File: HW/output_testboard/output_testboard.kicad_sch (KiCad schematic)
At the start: 50 parts, among them J1 IN, J2 OUT, J3 OUT, J4 DC_Jack, J5 9V, U1 TL072, U3 TL072

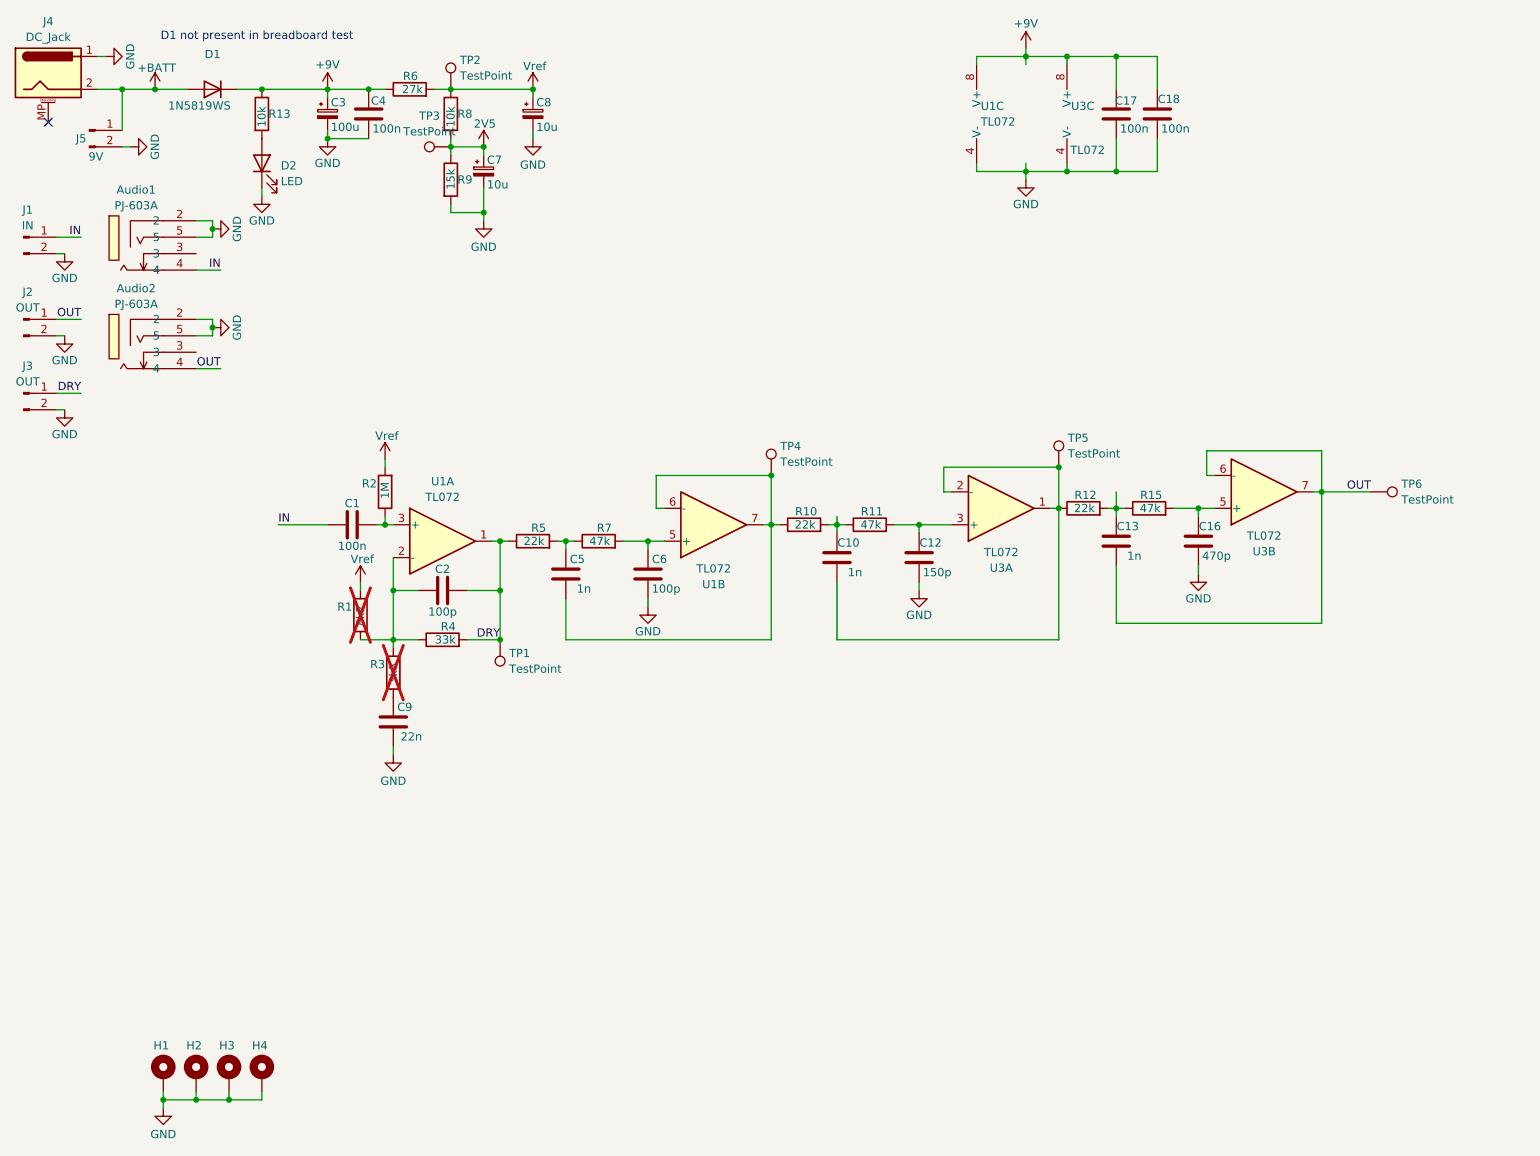
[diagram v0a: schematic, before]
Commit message: working passthrough code with dma + ouput buffer HW
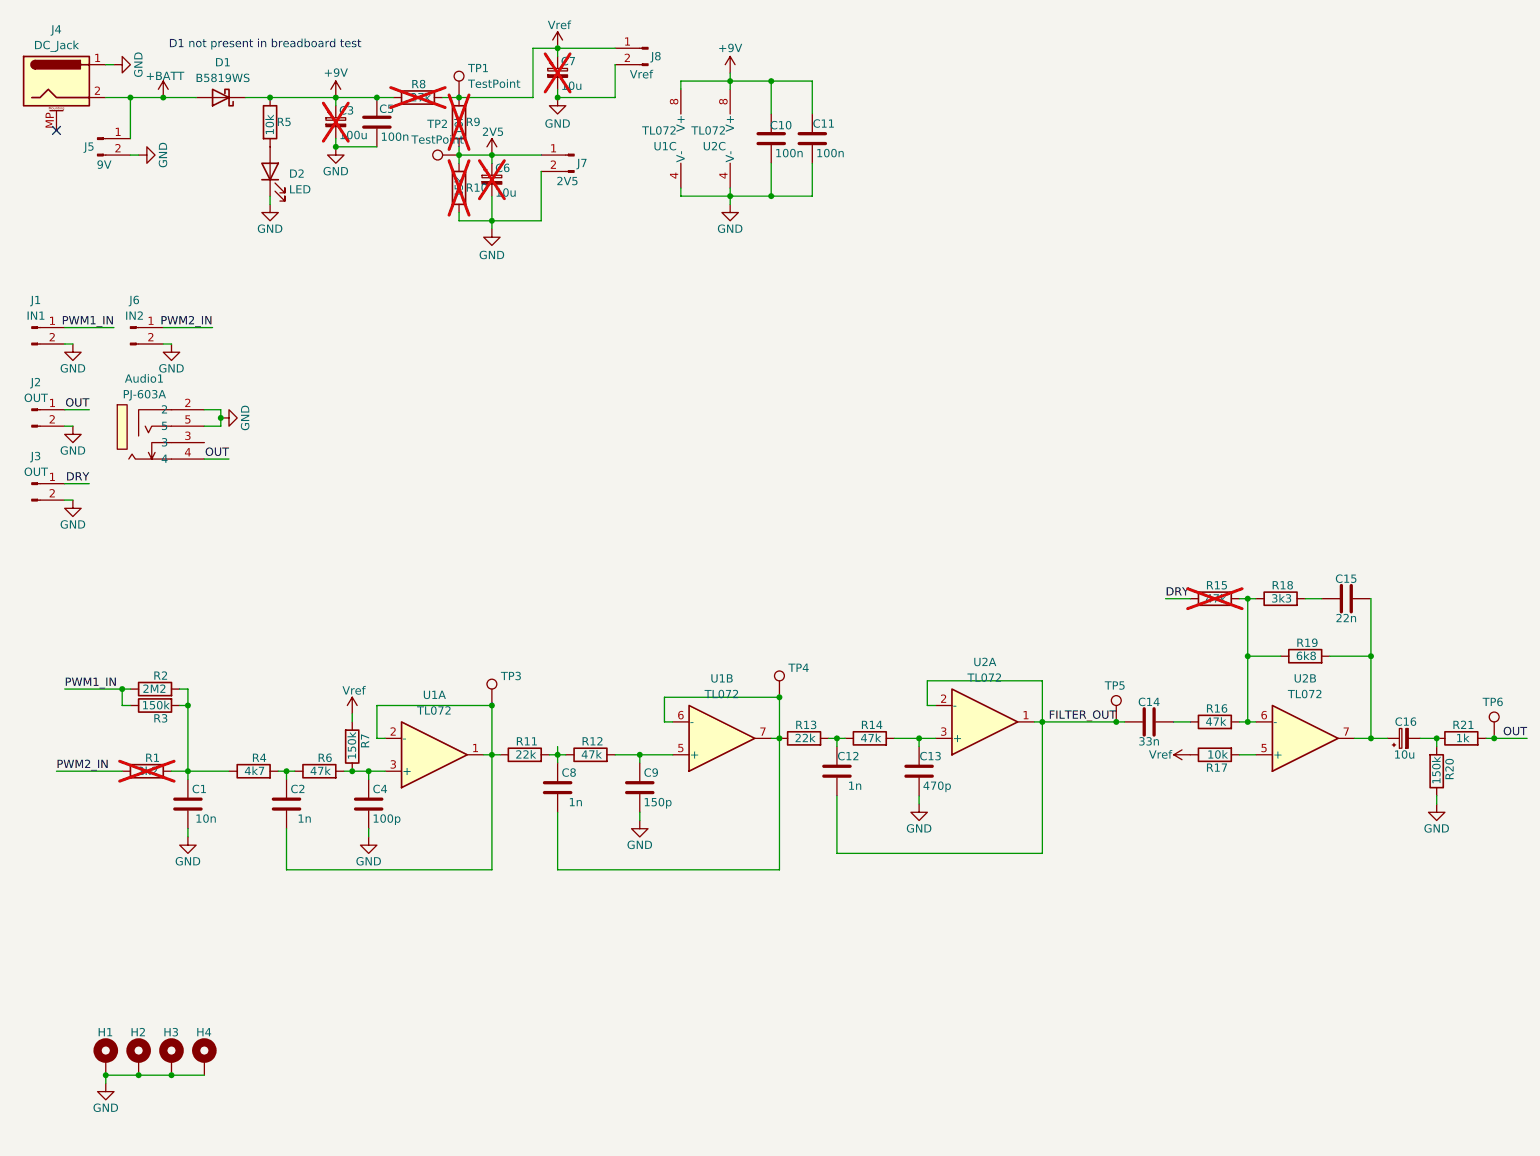
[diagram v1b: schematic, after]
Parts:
- removed Audio2: PJ-603A, AREA_lib_composant:AUDIO-TH_PJ-603A_1, symbol easyeda2kicad:PJ-603A
- removed C16: 470p, Capacitor_SMD:C_0603_1608Metric, symbol Device:C
- removed C17, C18: 100n, Capacitor_SMD:C_0603_1608Metric, symbol Device:C
- removed C6: 100p, Capacitor_SMD:C_0603_1608Metric, symbol Device:C
- removed C8: 10u, Capacitor_SMD:CP_Elec_5x5.4, symbol Device:C_Polarized_Small
- removed D1: 1N5819WS, Diode_SMD:D_SOD-323, symbol Device:D
- removed U3: TL072, Package_SO:SOIC-8_3.9x4.9mm_P1.27mm, symbol Amplifier_Operational:TL072
- added C11: 100n, Capacitor_SMD:C_0603_1608Metric, symbol Device:C
- added C14: 33n, Capacitor_SMD:C_0603_1608Metric, symbol Device:C
- added C15: 22n, Capacitor_SMD:C_0603_1608Metric, symbol Device:C
- added C16, C6: 10u, Capacitor_SMD:CP_Elec_5x5.4, symbol Device:C_Polarized_Small
- added C8: 1n, Capacitor_SMD:C_0603_1608Metric, symbol Device:C
- added D1: B5819WS, Diode_SMD:D_SOD-123, symbol Device:D_Schottky
- added J6: IN2, Connector_PinHeader_2.54mm:PinHeader_1x02_P2.54mm_Vertical, symbol Connector:Conn_01x02_Pin
- added J7: 2V5, Connector_PinHeader_2.54mm:PinHeader_1x02_P2.54mm_Vertical, symbol Connector:Conn_01x02_Pin
- added J8: Vref, Connector_PinHeader_2.54mm:PinHeader_1x02_P2.54mm_Vertical, symbol Connector:Conn_01x02_Pin
- added R14, R16: 47k, Resistor_SMD:R_0603_1608Metric, symbol Device:R
- added R17: 10k, Resistor_SMD:R_0603_1608Metric, symbol Device:R
- added R18: 3k3, Resistor_SMD:R_0603_1608Metric, symbol Device:R
- added R19: 6k8, Resistor_SMD:R_0603_1608Metric, symbol Device:R
- added R20: 150k, Resistor_SMD:R_0603_1608Metric, symbol Device:R
- added R21: 1k, Resistor_SMD:R_0603_1608Metric, symbol Device:R
- added U2: TL072, Package_SO:SOIC-8_3.9x4.9mm_P1.27mm, symbol Amplifier_Operational:TL072
- C1: value 100n -> 10n
- C10, C5: value 1n -> 100n
- C12: value 150p -> 1n
- C13: value 1n -> 470p
- C2: value 100p -> 1n
- C3, C7, R15: now not fitted
- C4: value 100n -> 100p
- C9: value 22n -> 150p
- H1, H2, H3, H4: value ~ -> MountingHole_Pad
- J1: value IN -> IN1; footprint Connector_JST:JST_PH_B2B-PH-K_1x02_P2.00mm_Vertical -> Connector_PinHeader_2.54mm:PinHeader_1x02_P2.54mm_Vertical
- J2, J3, J5: footprint Connector_JST:JST_PH_B2B-PH-K_1x02_P2.00mm_Vertical -> Connector_PinHeader_2.54mm:PinHeader_1x02_P2.54mm_Vertical
- R1: value 8k2 -> 2k2
- R10: value 22k -> 15k; now not fitted
- R11: value 47k -> 22k
- R12: value 22k -> 47k
- R13: value 10k -> 22k
- R2: value 1M -> 2M2
- R3: value 3k3 -> 150k; now fitted
- R4: value 33k -> 4k7
- R5: value 22k -> 10k
- R6: value 27k -> 47k
- R7: value 47k -> 150k
- R8: value 10k -> 27k; now not fitted
- R9: value 15k -> 10k; now not fitted
- TP1, TP2, TP3, TP4, TP5, TP6: footprint TestPoint:TestPoint_Pad_D1.0mm -> TestPoint:TestPoint_Plated_Hole_D2.0mm
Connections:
- net +9V: now also C10.1, C5.1, R5.1, R8.1, C11.1, D1.1 (K), U2.8 (V+); no longer C4.1, R13.1, R6.1
- net +BATT: now also D1.2 (A)
- net 2V5: now also R10.1, R9.2, TP2.1, C6.1, J7.1 (Pin_1); no longer C7.1, R8.2, R9.1, TP3.1
- net DRY: now also R15.1; no longer C2.2, R4.2, R5.1, TP1.1, U1.1
- net GND: now also C1.2, C10.2, C13.2, C5.2, R10.2, C11.2, C6.2, J6.2 (Pin_2), J7.2 (Pin_2), J8.2 (Pin_2), R20.1, U2.4 (V-); no longer C12.2, R9.2
- net OUT: now also Audio1.4, R21.2; no longer C13.2
- net Vref: now also C7.1, R7.2, R8.2, R9.1, TP1.1, J8.1 (Pin_1), R17.1; no longer R1.2, R2.2, R6.2, R8.1, TP2.1
- net at C9.1: now also R12.2, U1.5 (+); no longer R3.1
- net at R15.2: now also R16.2, R18.1, R19.1, U2.6 (-)
- net at R11.2: now also R12.1, C8.1; no longer C12.1
- net at TP4.1, U1.6 (-), U1.7: now also R13.1, C8.2; no longer C5.2, R10.1
- net at R13.2: now also C12.1, R14.1; no longer D2.2 (A)
- removed net IN: Audio1.4, C1.1, J1.1 (Pin_1)
- new net: C1.1, R1.2, R2.2, R3.2, R4.1
- new net: C2.1, R4.2, R6.1
- new net: C2.2, R11.1, TP3.1, U1.1, U1.2 (-)
- new net: C4.1, R6.2, R7.1, U1.3 (+)
- new net: C16.2, R20.2, R21.1
- new net: C14.2, R16.1
- new net: R17.2, U2.5 (+)
- new net: C13.1, R14.2, U2.3 (+)
- new net: C15.1, R18.2
- new net: C15.2, C16.1, R19.2, U2.7
- new net: D2.2 (A), R5.2
- new net FILTER_OUT: C12.2, C14.1, TP5.1, U2.1, U2.2 (-)
- new net PWM1_IN: J1.1 (Pin_1), R2.1, R3.1
- new net PWM2_IN: J6.1 (Pin_1), R1.1

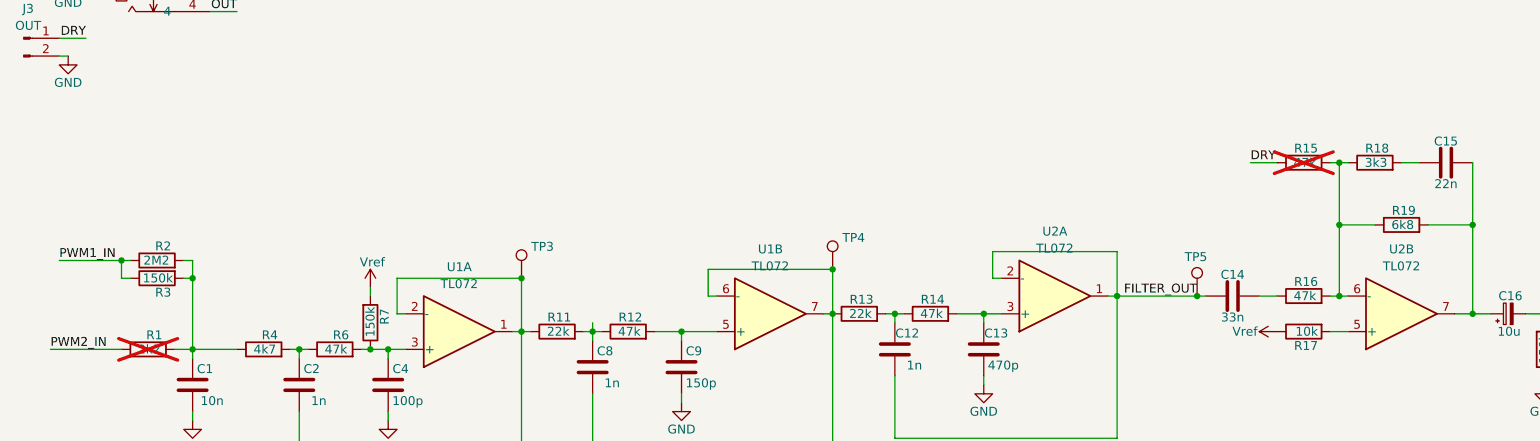
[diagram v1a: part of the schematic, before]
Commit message: correction on output board and new main layout/schem
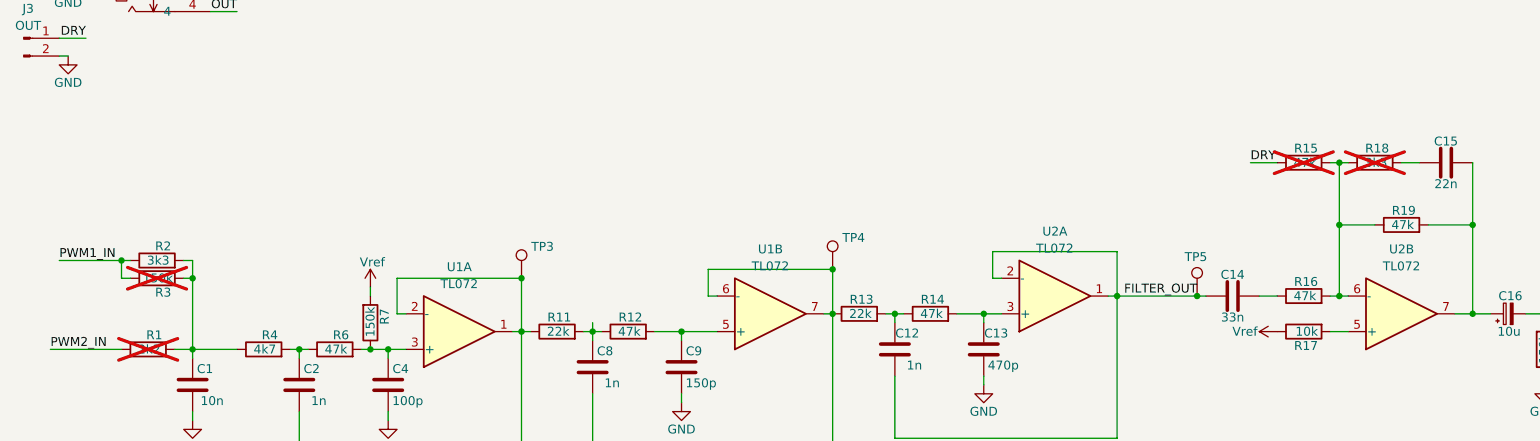
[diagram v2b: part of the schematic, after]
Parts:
- R18, R3: now not fitted
- R19: value 6k8 -> 47k
- R2: value 2M2 -> 3k3
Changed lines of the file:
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@@
 			)
 		)
-		(property "Value" "2M2"
+		(property "Value" "3k3"
 			(at 38.608 118.11 90)
 			(effects
@@
 		(in_bom yes)
 		(on_board yes)
-		(dnp no)
+		(dnp yes)
 		(property "Reference" "R18"
 			(at 212.852 102.108 90)
@@
 			)
 		)
-		(property "Value" "6k8"
+		(property "Value" "47k"
 			(at 216.408 113.03 90)
 			(effects
@@
 		(in_bom yes)
 		(on_board yes)
-		(dnp no)
+		(dnp yes)
 		(property "Reference" "R3"
 			(at 38.862 122.682 90)
